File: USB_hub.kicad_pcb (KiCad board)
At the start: 6 copper layers, 108.9 x 104.3 mm, 310 parts, among them J1 USB_SPI_(Opt), J10 USB3_A, J11 8-pin ATX connector, J12 USB_C_Receptacle, J13 I2C_HD3SS3220, J2 USB_C_Receptacle, J3 I2C_HD3SS3220, J4 USB_C_Receptacle, J5 I2C2_PD_Controller, J6 I2C_Mux, J7 I2C_EEPROM, J8 SD_Card_Receptacle, J9 USB3_A, Q1 MMBT2222A, SW1 RESET_HUB, SW2 FW_Upgrade, U1 USB7206C/KDX, U10 24LC256, U11 TPD4E02B04DQA, U12 TPD4E02B04DQA, U13 TPD4E02B04DQA, U14 TUSB1142IRNQR_C5216209, U15 GL3224-OIY04, U16 TPD4E02B04DQA, U17 TPD4E02B04DQA, U18 UCS2114-1-V/G4, U19 TPD4E02B04DQA, U2 MIC803-29D4VM3-TR, U20 TPD4E02B04DQA, U21 SiRA80DP, U22 TPS25983, U23 AP7361C-33E, U24 MP8795, U25 MIC23201YML-TR, U26 HD3SS3220IRNHR, U27 TPD4E02B04DQA, U28 TPD4E02B04DQA, U29 TPD4E02B04DQA, U3 HD3SS3220IRNHR, U32 TPD4E02B04DQA, U4 TPS2068EDBVR, U5 TPD4E02B04DQA, U6 TPD4E02B04DQA, U7 TPD4E02B04DQA, U8 TVS2200DRV, U9 TPS25762CQRQLRQ1, Y1 25MHz, Y2 25MHz +-0.03%

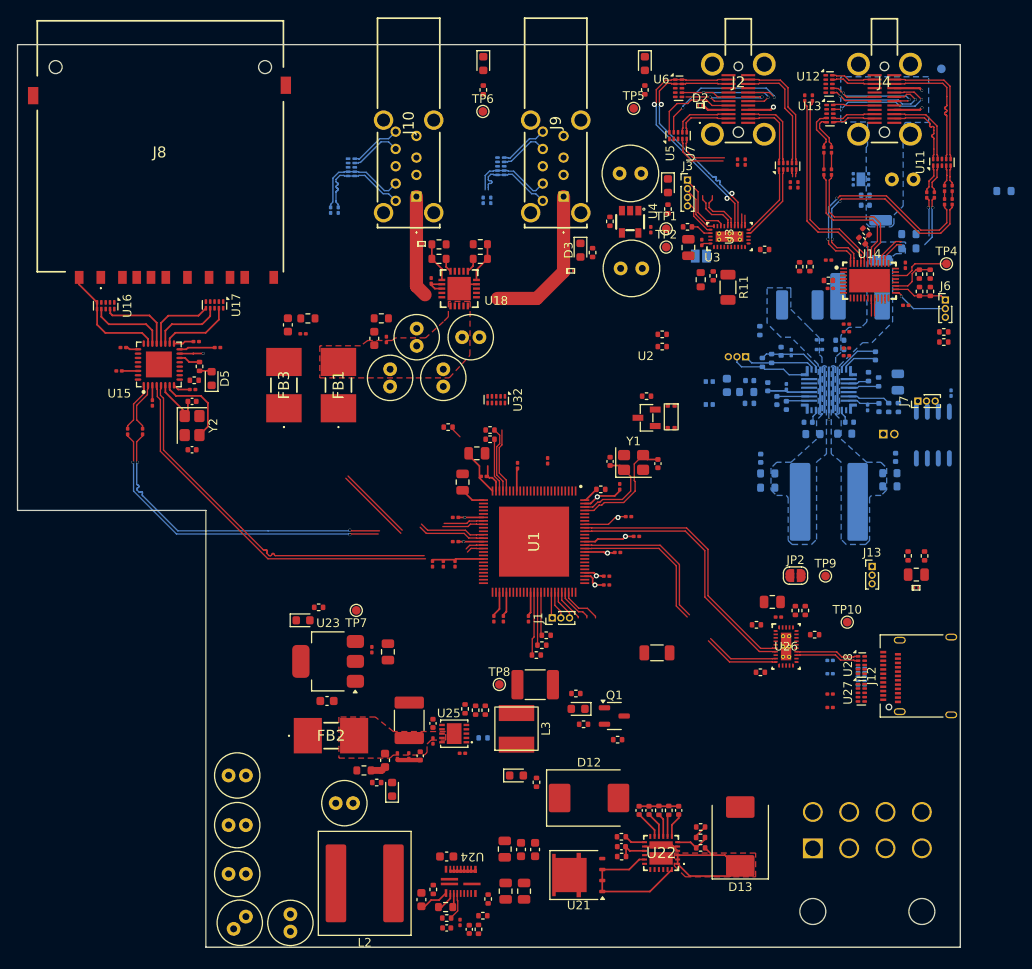
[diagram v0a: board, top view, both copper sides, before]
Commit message: Design rule file added, lots of minor tweaks, routing done (including differential pairs), DRC done/
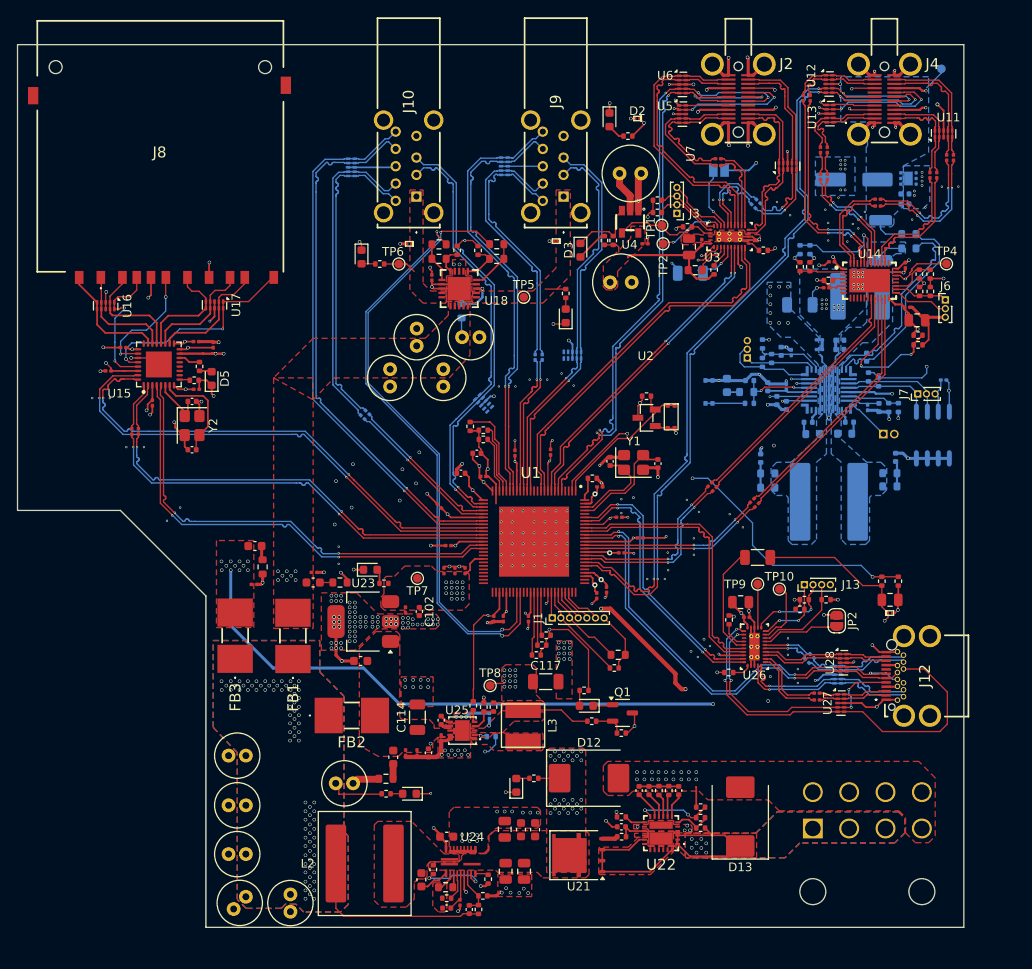
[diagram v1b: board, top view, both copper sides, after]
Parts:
- removed NT1: NetTie_2, Resistor_SMD:R_0603_1608Metric
- added R100: 10k, Resistor_SMD:R_0402_1005Metric, F.Cu at (88.3, 48.0)
- added R101: 10k, Resistor_SMD:R_0402_1005Metric, F.Cu at (90.7, 48.0)
- added R102: 0, Resistor_SMD:R_0603_1608Metric, B.Cu at (88.8, 55.0)
- added R103: 200k, Resistor_SMD:R_0402_1005Metric, F.Cu at (106.4, 96.3)
- added R104: 10, Resistor_SMD:R_0603_1608Metric, F.Cu at (106.9, 94.7)
- added U32: TPD4E02B04DQA, Package_SON:USON-10_2.5x1.0mm_P0.5mm, B.Cu at (101.6, 60.1)
- C10, C102, C19: value 4.7uF -> 4.7uF 10V; footprint Capacitor_SMD:C_0805_2012Metric -> Capacitor_SMD:C_0402_1005Metric
- C112, C122, C123, C124, C125, C126, C127, C128, C129, C130, C24, C25, C26, C66, C67, C68, C69, C70, C71, C72, C73, C76, C77: value 100nF -> 0.1uF
- C114, C117: value 22uF -> 22uF 40V; footprint Capacitor_SMD:C_1812_4532Metric -> Capacitor_SMD:C_1206_3216Metric
- C118, R11, R54, R56: moved to B.Cu
- C121, C23: value 100uF -> 100uF (6.3V)
- C27, C28: value 100nF -> 0.1uF; moved to B.Cu
- C32, C34: value 4.7uF 6.3V -> 4.7uF 10V
- C38: footprint Capacitor_SMD:C_1812_4532Metric -> Capacitor_SMD:C_1206_3216Metric
- C45: value 0.1uF 40V -> 0.1uF (50V)
- C51: footprint Capacitor_THT:C_Radial_D6.3mm_H11.0mm_P2.50mm -> Capacitor_SMD:CP_Elec_6.3x7.7
- C65: moved to F.Cu
- J1: footprint Connector_PinHeader_1.00mm:PinHeader_1x03_P1.00mm_Vertical -> Connector_PinHeader_1.00mm:PinHeader_1x07_P1.00mm_Vertical
- J12: footprint Connector_USB:USB_C_Receptacle_Amphenol_12401610E4-2A -> SamacSys_Parts:DX07S024XJ1R1100
- J13: footprint Connector_PinHeader_1.00mm:PinHeader_1x03_P1.00mm_Vertical -> Connector_PinHeader_1.00mm:PinHeader_1x04_P1.00mm_Vertical
- R27, R31: value 10 (0.1W) -> 10 (0.25W)
- R79: value 680 -> 680 1%
- U18: value UCS2114-1-V/G4 -> UCS2113
- U23: value AP7361C-33E -> AP7361C-33E-13
- U33: renamed from U32; moved to B.Cu
- Y1: value 25MHz -> 25MHz +-0.03%
- moved R68 30.9 mm to (74.7, 86.4)
- moved D6 30.6 mm to (100.8, 55.6), turned to 90 degrees
- moved FB3 29.5 mm to (62.6, 92.5)
- moved C94 29.5 mm to (64.8, 86.6)
- moved FB1 29.5 mm to (69.3, 92.6)
- moved R75 29.2 mm to (65.8, 84.6), turned to -90 degrees
- moved C85 29.1 mm to (71.6, 86.4), turned to 0 degrees
- moved C86 28.2 mm to (71.8, 85.2), turned to 0 degrees
- moved D7 26.4 mm to (77.2, 48.8)
- moved C93 25.8 mm to (64.9, 82.2), turned to 0 degrees
- moved TP5 25.2 mm to (96.0, 53.4)
- moved R64 25.2 mm to (100.8, 53.0), turned to -90 degrees
- moved C61 24.3 mm to (117.5, 75.1), turned to 45 degrees
- moved C128 24.2 mm to (77.3, 67.3), turned to 135 degrees
- moved C62 23.7 mm to (118.0, 75.6), turned to 45 degrees
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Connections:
- net Net-(C57-Pad2) renamed /USB-C2/CTX2_R+
- net Net-(C58-Pad2) renamed /USB-C2/CTX2_R-
- net Net-(C59-Pad2) renamed /USB-C2/CTX1_R+
- net Net-(C60-Pad2) renamed /USB-C2/CTX1_R-
- net Net-(U26-TX1N) renamed /USB-C_UP1/TX1+
- net Net-(U26-TX1P) renamed /USB-C_UP1/TX1-
- net Net-(U26-TX2N) renamed /USB-C_UP1/TX2+
- net Net-(U26-TX2P) renamed /USB-C_UP1/TX2-
- net Net-(U9-CSN/BUS) renamed /USB-C2/CSN
- net Net-(U9-CSP) renamed /USB-C2/CSP
- net Net-(U9-OUT) renamed /USB-C2/CS_1P
- C123 pad 2: unconnected-(C123-Pad2) -> /USB-C_UP1/USB-C1.TX1-
- C36 pad 2: PGND -> GND
- C37 pad 2: PGND -> GND
- C41 pad 2: PGND -> GND
- C43 pad 2: PGND -> GND
- C45 pad 2: PGND -> GND
- C47 pad 2: PGND -> GND
- C48 pad 2: PGND -> GND
- C49 pad 2: PGND -> GND
- C50 pad 2: PGND -> GND
- C51 pad 2: PGND -> GND
- C52 pad 2: PGND -> GND
- C53 pad 2: PGND -> GND
- J10 pad MH1: (no net) -> GND
- J10 pad MH4: (no net) -> GND
- J2 pad MH1: (no net) -> GND
- J2 pad MH2: (no net) -> GND
- J2 pad MH3: (no net) -> GND
- J2 pad MH4: (no net) -> GND
- J4 pad A1: PGND -> GND
- J4 pad A12: PGND -> GND
- J4 pad B1: PGND -> GND
- J4 pad B12: PGND -> GND
- J4 pad MH1: (no net) -> GND
- J4 pad MH2: (no net) -> GND
- J4 pad MH3: (no net) -> GND
- J4 pad MH4: (no net) -> GND
- J9 pad MH1: (no net) -> GND
- J9 pad MH2: (no net) -> GND
- J9 pad MH3: (no net) -> GND
- J9 pad MH4: (no net) -> GND
- R92 pad 2: VBUS_C1 -> VBUS_UP
- SW2 pad 1: PGND -> GND
- U1 pad 8: /USB-C1/USB3_IN.TX1+ -> /USB-C1/USB3_IN.TX1-
- U18 pad 13: +5V_USB_A -> /USB-A1/COMM_ILIM
- U22 pad 16: (no net) -> Net-(D13-C)
- U22 pad 25: Net-(U21-S-Pad1) -> Net-(D13-C)
- U26 pad 14: /USB-C_UP1/USB-C1.RX1- -> /USB-C_UP1/USB-C1.RX1+
- U26 pad 15: /USB-C_UP1/USB-C1.RX1+ -> /USB-C_UP1/USB-C1.RX1-
- U27 pad 1: /USB-C_UP1/USB-C1.CC1 -> /USB-C_UP1/USB-C1.TX1-
- U27 pad 10: /USB-C_UP1/USB-C1.CC1 -> /USB-C_UP1/USB-C1.TX1-
- U27 pad 2: /USB-C_UP1/USB-C1.CC2 -> /USB-C_UP1/USB-C1.TX1+
- U27 pad 4: /USB-C_UP1/USB-C1.TX1- -> /USB-C_UP1/USB-C1.CC1
- U27 pad 5: /USB-C_UP1/USB-C1.TX1+ -> /USB-C_UP1/USB-C1.CC2
- U27 pad 6: /USB-C_UP1/USB-C1.TX1+ -> /USB-C_UP1/USB-C1.CC2
- U27 pad 7: /USB-C_UP1/USB-C1.TX1- -> /USB-C_UP1/USB-C1.CC1
- U27 pad 9: /USB-C_UP1/USB-C1.CC2 -> /USB-C_UP1/USB-C1.TX1+
- U3 pad 10: /USB-C1/USB3_IN.RX1- -> /USB-C1/USB3_IN.RX1+
- U3 pad 6: /USB-C1/USB3_IN.TX1+ -> /USB-C1/USB3_IN.TX1-
- U3 pad 7: /USB-C1/USB3_IN.TX1- -> /USB-C1/USB3_IN.TX1+
- U3 pad 9: /USB-C1/USB3_IN.RX1+ -> /USB-C1/USB3_IN.RX1-
- U33 pad 1: /USB-A1/USB-A1.D+ -> Net-(U33-IO1)
- U33 pad 10: /USB-A1/USB-A1.D+ -> Net-(U33-IO1)
- U33 pad 2: /USB-A1/USB-A1.D- -> Net-(U33-IO2)
- U33 pad 4: /USB-A1/USB-A2.D- -> /USB-A1/USB-A2.D+
- U33 pad 5: /USB-A1/USB-A2.D+ -> /USB-A1/USB-A2.D-
- U33 pad 6: /USB-A1/USB-A2.D+ -> /USB-A1/USB-A2.D-
- U33 pad 7: /USB-A1/USB-A2.D- -> /USB-A1/USB-A2.D+
- U33 pad 9: /USB-A1/USB-A1.D- -> Net-(U33-IO2)
- U8 pad 1: PGND -> GND
- U8 pad 2: PGND -> GND
- U8 pad 3: PGND -> GND
- U8 pad 7: PGND -> GND
- U9 pad 13: PGND -> GND
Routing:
- net GND: track 21.7 -> 310.3 mm, vias 0 -> 376
- net +3V3: track 27.0 -> 246.7 mm, vias 3 -> 42
- net +5V_USB_C_SD: track 3.81 -> 143.9 mm, vias 1 -> 16
- net /USB-C2/USB3_IN.D+: track 17.5 -> 97.3 mm, vias 2 -> 4
- net /USB-C2/USB3_IN.D-: track 15.2 -> 94.8 mm, vias 2 -> 4
- net /USB-A1/PRT_EN1: track 0.00 -> 70.2 mm, vias 0 -> 2
- net /USB-A1/PRT_EN2: track 0.00 -> 67.2 mm, vias 0 -> 2
- net /USB-C1/USB3_IN.D+: track 12.8 -> 71.1 mm, vias 2 -> 4
- net /SD-interface/USB-SD.D-: track 0.00 -> 58.1 mm, vias 0 -> 2
- net /SD-interface/USB-SD.D+: track 0.00 -> 58.0 mm, vias 0 -> 2
- net /USB-C1/USB3_IN.D-: track 15.8 -> 72.8 mm, vias 2 -> 4
- net /USB-C_UP1/USB3_IN.D-: track 0.00 -> 53.3 mm, vias 0 -> 3
- net /USB-C_UP1/USB3_IN.D+: track 0.00 -> 51.3 mm, vias 0 -> 2
- net /USB-A1/USB-A2.D+: track 0.00 -> 50.0 mm, vias 0 -> 1
- net /USB-A1/USB-A2.D-: track 0.00 -> 50.0 mm, vias 0 -> 1
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- added copper zone on B.Cu, net +12V
- added copper zone on F.Cu, net +12V
- added copper zone on In2.Cu, net +12V
- added copper zone on In3.Cu, net +12V
- added copper zone on In3.Cu, net +1V2_SD
- added copper zone on F.Cu, net +3V3
- added copper zone on In2.Cu, net +3V3
- added copper zone on In2.Cu, net +3V3_SD
- added copper zone on In2.Cu, net +5V_USB_A
- added copper zone on F.Cu, net +5V_USB_C_SD
- added copper zone on In3.Cu, net +5V_USB_C_SD
- added copper zone on B.Cu, net +5V_prefiltered
- added copper zone on F.Cu, net +5V_prefiltered
- added copper zone on In2.Cu, net +5V_prefiltered
- added copper zone on In3.Cu, net +5V_prefiltered
- added copper zone on F.Cu, net AGND
- added copper zone on B.Cu, net GND
- added copper zone on F.Cu, net GND
- added copper zone on B.Cu, net Net-(D13-C)
- added copper zone on In2.Cu, net Net-(D13-C)
- added copper zone on In3.Cu, net Net-(D13-C)
- added copper zone on F.Cu, net Net-(U21-S-Pad1)
- added copper zone on F.Cu, net Net-(U24-SW)
- added copper zone on F.Cu, net Net-(U25-SW)
- added copper zone on F.Cu, net VBUS-A1
- added copper zone on F.Cu, net VBUS-A2
- added copper zone on In2.Cu, net VBUS_C1
- added copper zone on In3.Cu, net VBUS_C1
- added copper zone on F.Cu, net VCORE
- added copper zone on In3.Cu, net VCORE
- removed copper zone on In2.Cu, net VCORE
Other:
- board size 108.9 x 104.3 mm -> 109.3 x 102 mm
- board text added: "Green traces are USB_SS differential pairs - 90 ohms"
- board text added: "Yellow traces are SD traces - 50 ohms"
